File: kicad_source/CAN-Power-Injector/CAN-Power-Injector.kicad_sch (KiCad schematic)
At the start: 45 parts, among them CN1 DNI, CN2 SM04B-GHS-TB, CN3 SM04B-GHS-TB, CN4 Powerpole_2, CN5 SM04B-GHS-TB, CN6 SM04B-GHS-TB, CN7 DNI, U1 RAA211650

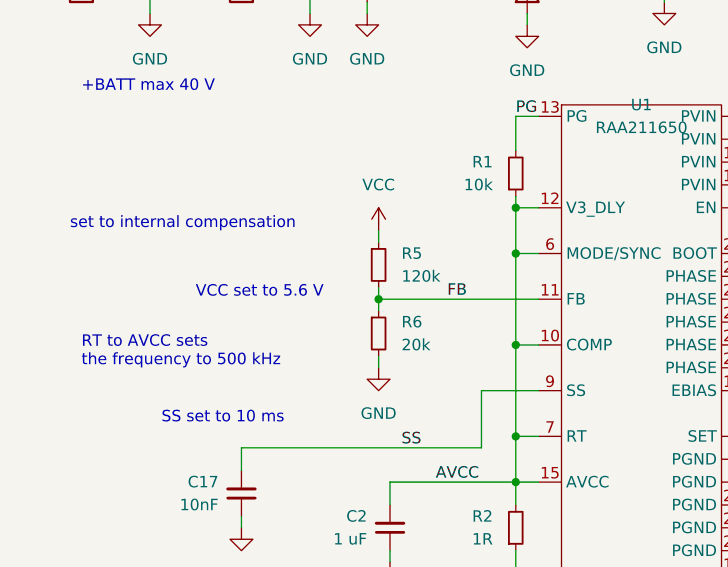
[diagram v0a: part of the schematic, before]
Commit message: changed R5 to 110 k. this changes VCC to 5.2V
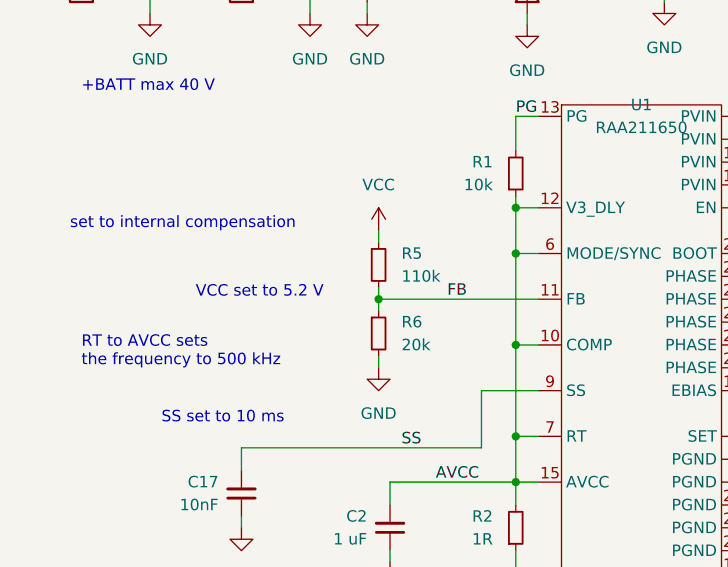
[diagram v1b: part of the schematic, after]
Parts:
- R5: value 120k -> 110k
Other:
- note added: "VCC set to 5.2 V"
- note removed: "VCC set to 5.6 V"
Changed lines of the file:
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@@
   (title_block
     (title "CAN-Power-Injector")
-    (date "2022-12-12")
-    (rev "0.1")
+    (date "2023-05-01")
+    (rev "0.1.1")
     (company "107-systems")
   )
@@
     (effects (font (size 1.27 1.27)) (justify left bottom))
   )
-  (text "VCC set to 5.6 V" (at 34.29 64.77 0)
+  (text "VCC set to 5.2 V" (at 34.29 64.77 0)
     (effects (font (size 1.27 1.27)) (justify left bottom))
   )
@@
       (effects (font (size 1.27 1.27)) (justify left))
     )
-    (property "Value" "120k" (id 1) (at 57.15 62.2299 0)
+    (property "Value" "110k" (id 1) (at 57.15 62.2299 0)
       (effects (font (size 1.27 1.27)) (justify left))
     )
@@
     )
     (path "/efa5b69a-6ade-4964-9f49-dce704c2cbaa"
-      (reference "R5") (unit 1) (value "120k") (footprint "Resistor_SMD:R_0603_1608Metric")
+      (reference "R5") (unit 1) (value "110k") (footprint "Resistor_SMD:R_0603_1608Metric")
     )
     (path "/71ec15c8-fc95-422b-90ce-e728a02a7d17"

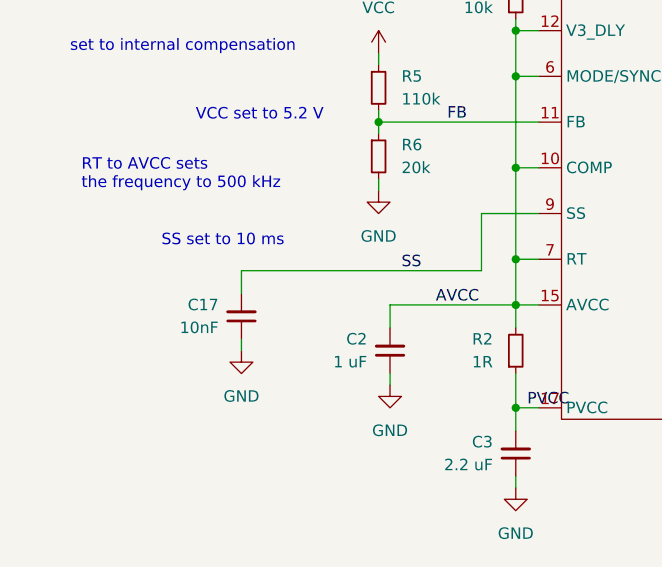
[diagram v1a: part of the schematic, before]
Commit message: increased C17 to 33 nF to achieve a soft start of 5.28 ms because of high output capacitance
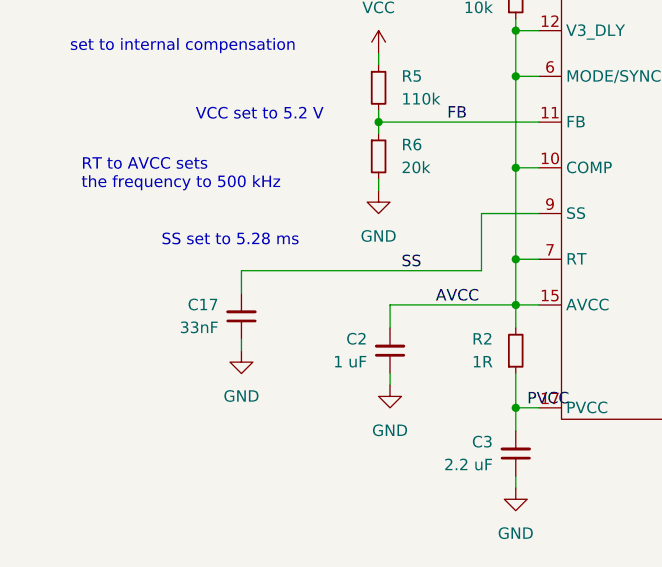
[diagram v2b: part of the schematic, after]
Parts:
- C17: value 10nF -> 33nF
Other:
- note added: "SS set to 5.28 ms"
- note removed: "SS set to 10 ms"
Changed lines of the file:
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@@
     (effects (font (size 1.27 1.27)) (justify left bottom))
   )
-  (text "SS set to 10 ms" (at 30.48 78.74 0)
+  (text "SS set to 5.28 ms" (at 30.48 78.74 0)
     (effects (font (size 1.27 1.27)) (justify left bottom))
   )
@@
       (effects (font (size 1.27 1.27)) (justify right))
     )
-    (property "Value" "10nF" (id 1) (at 36.83 87.6235 0)
+    (property "Value" "33nF" (id 1) (at 36.83 87.6235 0)
       (effects (font (size 1.27 1.27)) (justify right))
     )
@@
     )
     (path "/1b346cae-2c1b-4465-97a8-a36b5cf14b51"
-      (reference "C17") (unit 1) (value "10nF") (footprint "Capacitor_SMD:C_0603_1608Metric")
+      (reference "C17") (unit 1) (value "33nF") (footprint "Capacitor_SMD:C_0603_1608Metric")
     )
     (path "/fef5535b-a542-4028-a074-282a4f9c934c"
